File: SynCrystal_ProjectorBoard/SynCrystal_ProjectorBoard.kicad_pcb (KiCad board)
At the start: 2 copper layers, 54.4 x 23.5 mm, 28 parts, among them J1 to TCA955 PCB, J2 to DIN connecting 3+1 Socket 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, J3 to Lamp Relay Board, J4 to DIN Socket traces, J5 Relais Board, J6 uC Cable, Q1 AO3400A, U1 AP63205WU, U3 TS5A3160DBVR-TP, U4 TS5A3160DBVR-TP, U5 TSV911ILT

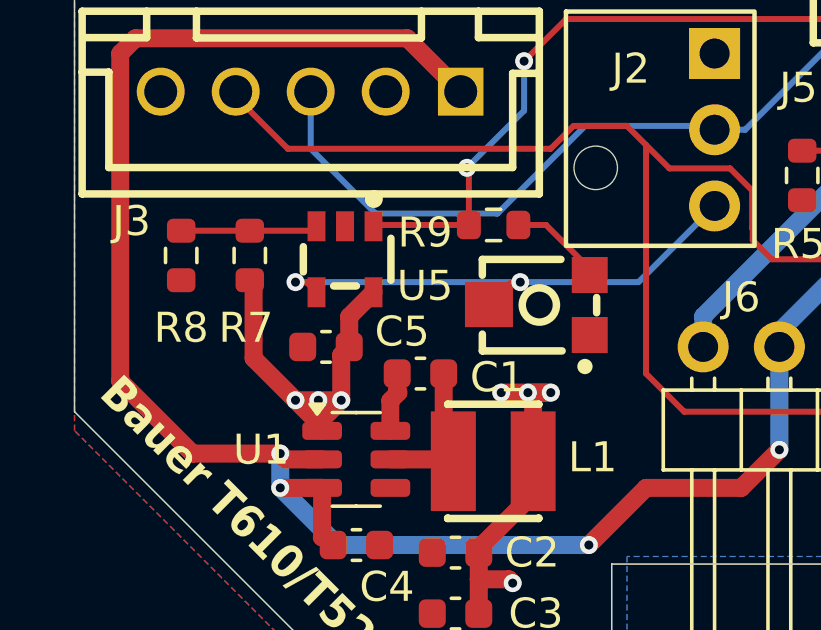
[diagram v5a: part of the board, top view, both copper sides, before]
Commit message: moving the 10k OpAmp Input R to the Projector board
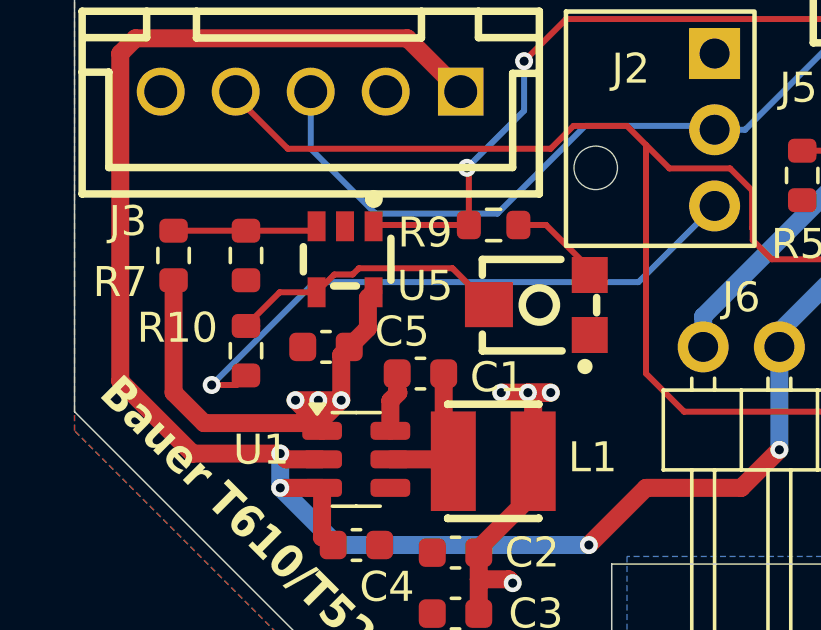
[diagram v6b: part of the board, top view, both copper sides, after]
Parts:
- added R10: 10k, Resistor_SMD:R_0603_1608Metric, F.Cu at (168.9, 88.1)
- moved R7 2.54 mm to (166.5, 85.0)
- moved R8 2.16 mm to (168.9, 85.0)
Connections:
- RV1 pad 2: /Ctrl_V_in -> Net-(U5--)
- U5 pad 4: /Ctrl_V_in -> Net-(U5--)
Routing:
- net Net-(U5--): track 0.00 -> 9.78 mm
- net +5V: track 30.3 -> 34.9 mm
- net /Ctrl_V_in: track 17.2 -> 20.5 mm, vias 2 -> 1

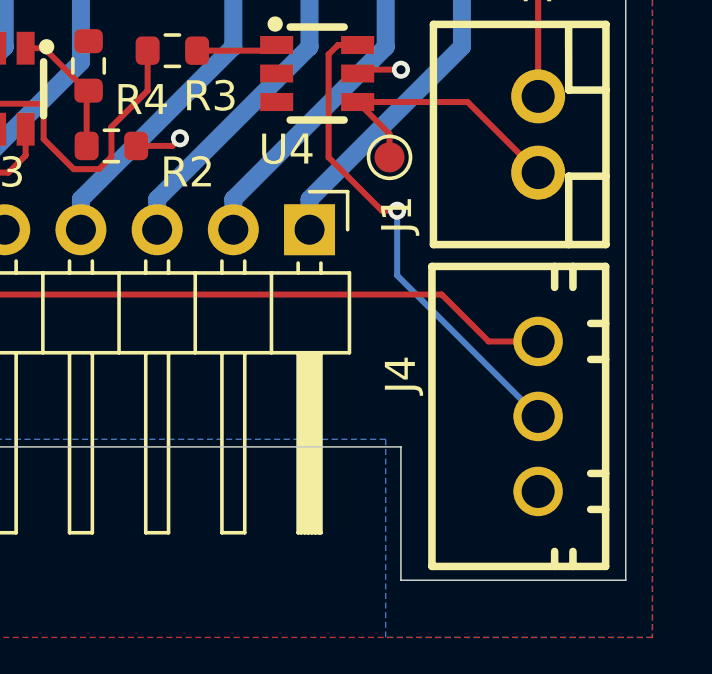
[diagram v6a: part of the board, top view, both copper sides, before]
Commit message: Adding the VOltage Divider to Projector Board to allow Projector Detection. Also, fixing various footprints on the controller. ERC now failing.
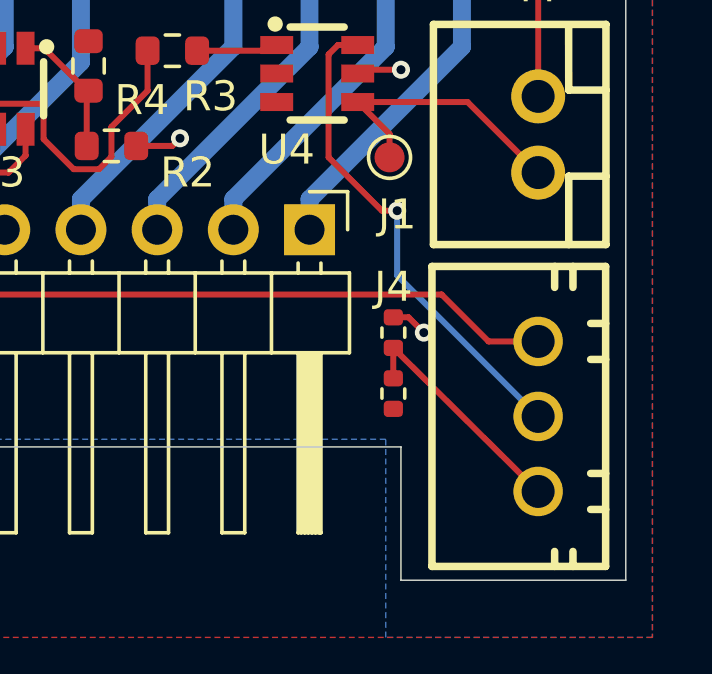
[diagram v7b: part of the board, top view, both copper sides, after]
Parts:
- added R11: 10k, Resistor_SMD:R_0402_1005Metric, F.Cu at (209.8, 93.5)
- added R12: 40k2, Resistor_SMD:R_0402_1005Metric, F.Cu at (209.8, 91.4)
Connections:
- J4 pad 3: GND -> Net-(J4-Pin_3)
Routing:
- net Net-(J4-Pin_3): track 0.00 -> 7.81 mm
- net +5V: track 34.9 -> 36.1 mm, vias 10 -> 11
